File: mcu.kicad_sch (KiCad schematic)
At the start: 15 parts, among them J3 PinHeader_2x05, U4 ISP1807-LR-RS, U5 D3V3XA4B10LP

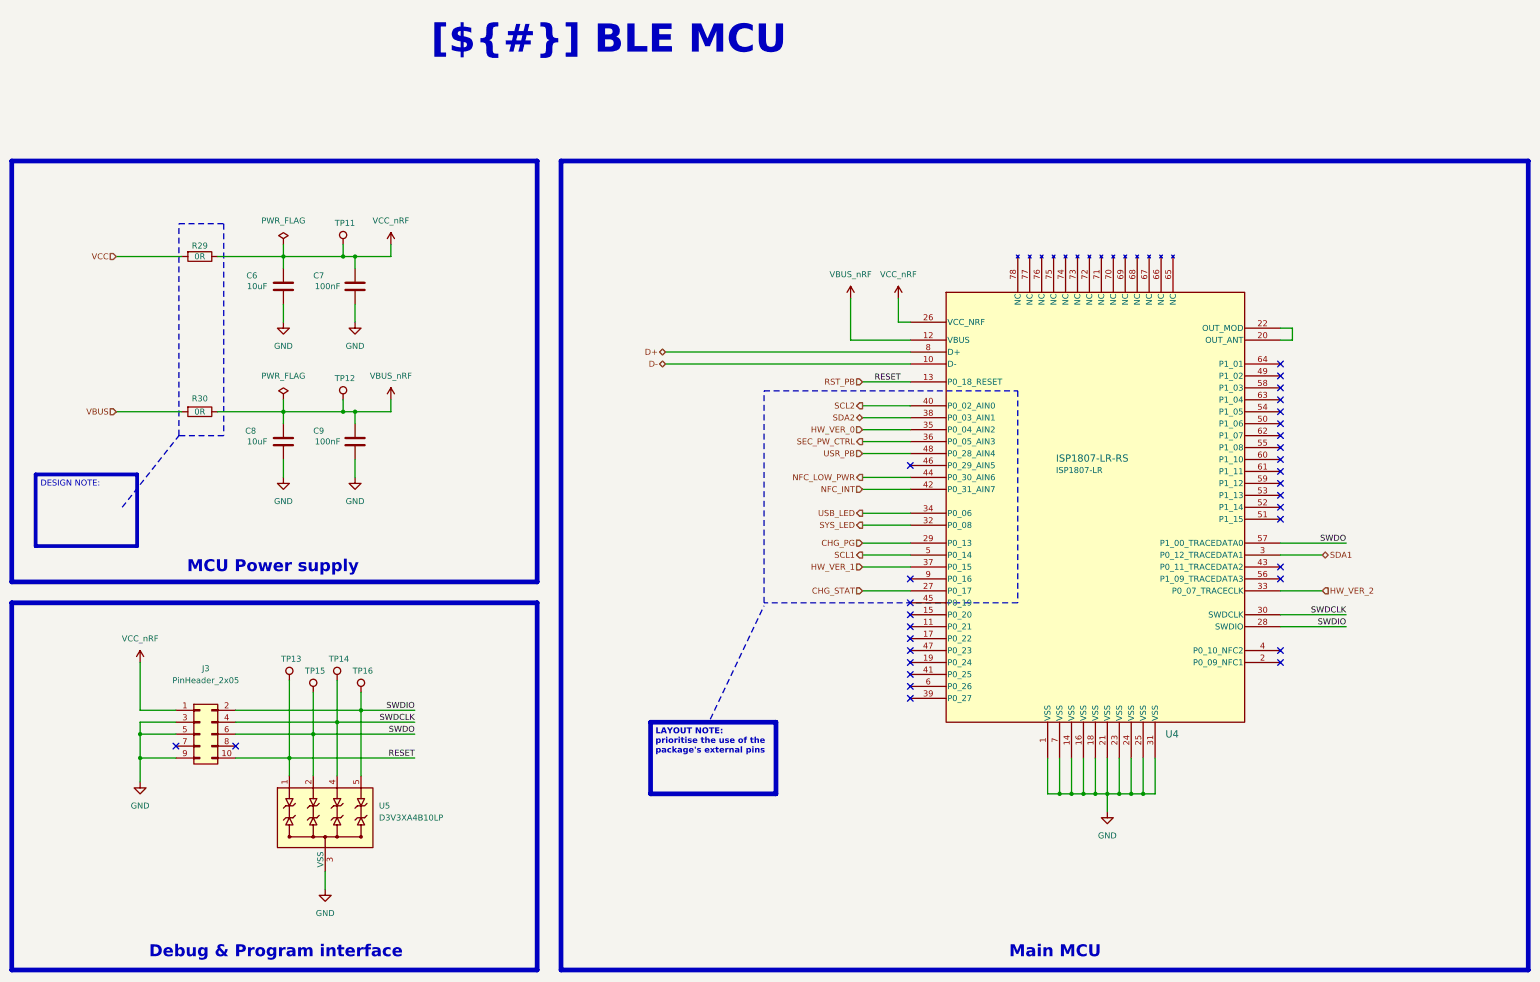
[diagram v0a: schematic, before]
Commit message: fix(hardware): replace jumper/passive footprints with 0402 and refine schematics
- Replace 0-ohm jumper resistors with 0402 package equivalents
- Reduce package size on several capacitors
- Correct and simplify several schematic symbols (replaced with
  simplified equivalents where the original was overcomplicated)
- Bump lib submodule to the updated component library (renamed
  switch footprints, new Conn_01x02_MountingPin symbol, pad/pin
  numbering fixes, approved IPN assignments, Workart artwork library)
- Register Workart.pretty in fp-lib-table
- Mark J3 as DNP in mcu.kicad_sch
- Continue schematic wiring/placement (Leds.kicad_sch, tessera.kicad_sch)
  and PCB routing/placement (tessera.kicad_pcb)
- Add board outline source (Images/pcb_size.dxf, pcb_shape.FCStd) and
  silkscreen artwork sources (Logos/) for the Workart footprints
- Complete preliminary version of PCB
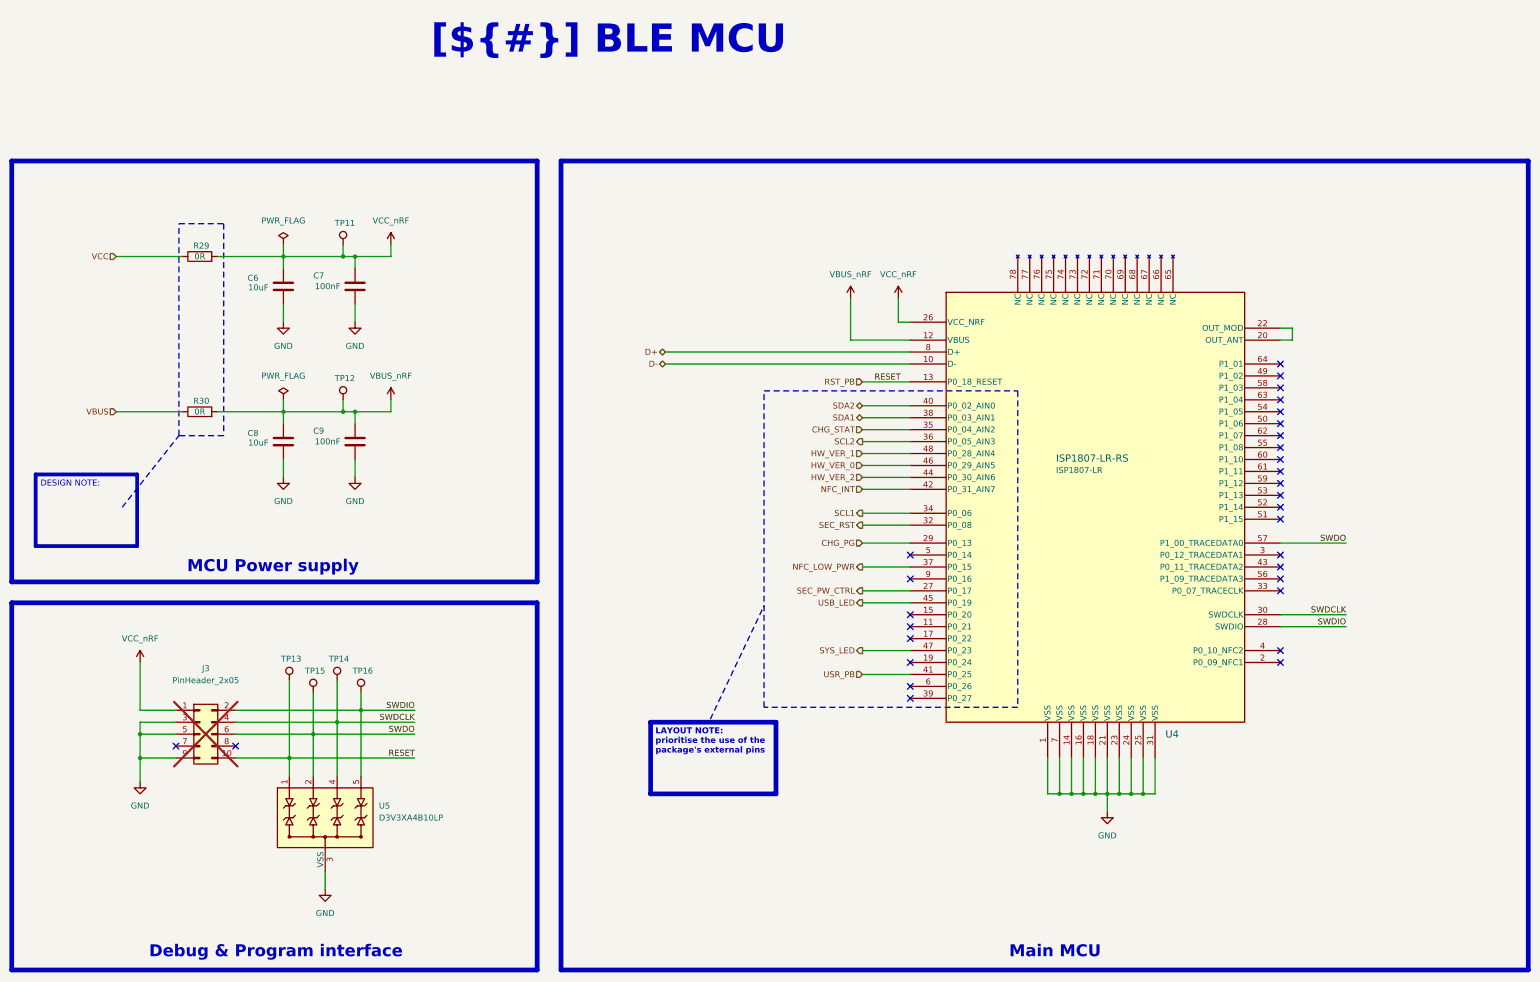
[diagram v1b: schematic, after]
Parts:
- removed C6, C8: 10uF 50V (X7R), Capacitor_SMD:C_1210_3225Metric, symbol catalog:Capacitors/C1210_10uF_50V_±10%_X7R
- removed R29, R30: 0R ±5% 1/10W, Resistor_SMD:R_0603_1608Metric, symbol catalog:Resistors/R0603_0R_0.1W_±5%
- added C6, C8: 10uF 10V (X7R), Capacitor_SMD:C_0805_2012Metric, symbol catalog:Capacitors/C0805_10uF_10V_±10%_X7R
- added R29, R30: 0R ±5% 1/16W, Resistor_SMD:R_0402_1005Metric, symbol catalog:Resistors/R0402_0R_0.1W_±5%
- J3: now not fitted
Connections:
- net CHG_STAT: now also U4.35 (P0_04_AIN2); no longer U4.27 (P0_17)
- net GND: now also C6.2, C8.2
- net HW_VER_0: now also U4.46 (P0_29_AIN5); no longer U4.35 (P0_04_AIN2)
- net HW_VER_1: now also U4.48 (P0_28_AIN4); no longer U4.37 (P0_15)
- net HW_VER_2: now also U4.44 (P0_30_AIN6); no longer U4.33 (P0_07_TRACECLK)
- net NFC_LOW_PWR: now also U4.37 (P0_15); no longer U4.44 (P0_30_AIN6)
- net SCL1: now also U4.34 (P0_06); no longer U4.5 (P0_14)
- net SCL2: now also U4.36 (P0_05_AIN3); no longer U4.40 (P0_02_AIN0)
- net SDA1: now also U4.38 (P0_03_AIN1); no longer U4.3 (P0_12_TRACEDATA1)
- net SDA2: now also U4.40 (P0_02_AIN0); no longer U4.38 (P0_03_AIN1)
- net SEC_PW_CTRL: now also U4.27 (P0_17); no longer U4.36 (P0_05_AIN3)
- net SWDIO: now also U5.6; no longer U5.10
- net SYS_LED: now also U4.47 (P0_23); no longer U4.32 (P0_08)
- net USB_LED: now also U4.45 (P0_19); no longer U4.34 (P0_06)
- net USR_PB: now also U4.41 (P0_25); no longer U4.48 (P0_28_AIN4)
- net VBUS: now also R30.1
- net VBUS_nRF: now also C8.1, R30.2
- net VCC: now also R29.1
- net VCC_nRF: now also C6.1, R29.2
- new net SEC_RST: U4.32 (P0_08)
- no-connect marks 31 -> 30

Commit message: feat(hardware): route debug UART to J3 and add charger status pull-ups
Exposes a spare UART on the SWD header for firmware logging and adds
external pull-ups to the BQ25170 open-drain status outputs.

- Route P0.22 (UART_TX) to J3 pin 7 and P0.20 (UART_RX) to J3 pin 8.
- Add R44/R45 100k pull-ups to VCC on CHG_STAT and CHG_PG.
- Update PCB placement and routing for the new nets.
- Bump lib submodule (new THT test point footprint).
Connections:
- net UART_RX: now reaches U4.15 (P0_20)
- net UART_RX: now also J3.8 (Pin_8)
- net UART_TX: now reaches U4.17 (P0_22)
- net UART_TX: now also J3.7 (Pin_7)
- no-connect marks 30 -> 26
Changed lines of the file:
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@@
 	(title_block
 		(title "BLE MCU")
-		(date "2026-10-03")
+		(date "2026-10-11")
 	)
 	(junction
@@
 	)
 	(no_connect
-		(at 245.11 158.75)
-	)
-	(no_connect
 		(at 323.85 143.51)
 	)
@@
 	)
 	(no_connect
-		(at 88.9 181.61)
-	)
-	(no_connect
 		(at 323.85 107.95)
 	)
@@
 	)
 	(no_connect
-		(at 101.6 181.61)
-	)
-	(no_connect
 		(at 245.11 163.83)
 	)
 	(no_connect
-		(at 245.11 153.67)
-	)
-	(no_connect
 		(at 323.85 102.87)
 	)
@@
 	(wire
 		(pts
-			(xy 234.95 134.62) (xy 245.11 134.62)
-		)
-		(stroke
-			(width 0)
-			(type default)
-		)
-	)
-	(wire
-		(pts
-			(xy 234.95 143.51) (xy 245.11 143.51)
+			(xy 232.41 134.62) (xy 245.11 134.62)
+		)
+		(stroke
+			(width 0)
+			(type default)
+		)
+	)
+	(wire
+		(pts
+			(xy 232.41 143.51) (xy 245.11 143.51)
 		)
 		(stroke
@@
 	(wire
 		(pts
-			(xy 234.95 151.13) (xy 245.11 151.13)
+			(xy 232.41 151.13) (xy 245.11 151.13)
+		)
+		(stroke
+			(width 0)
+			(type default)
+		)
+	)
+	(wire
+		(pts
+			(xy 69.85 181.61) (xy 88.9 181.61)
 		)
 		(stroke
@@
 	(wire
 		(pts
-			(xy 245.11 124.46) (xy 234.95 124.46)
+			(xy 245.11 124.46) (xy 232.41 124.46)
 		)
 		(stroke
@@
 	(wire
 		(pts
-			(xy 234.95 116.84) (xy 245.11 116.84)
-		)
-		(stroke
-			(width 0)
-			(type default)
-		)
-	)
-	(wire
-		(pts
-			(xy 234.95 119.38) (xy 245.11 119.38)
+			(xy 232.41 116.84) (xy 245.11 116.84)
+		)
+		(stroke
+			(width 0)
+			(type default)
+		)
+	)
+	(wire
+		(pts
+			(xy 232.41 119.38) (xy 245.11 119.38)
 		)
 		(stroke
@@
 	(wire
 		(pts
-			(xy 234.95 161.29) (xy 245.11 161.29)
+			(xy 232.41 161.29) (xy 245.11 161.29)
 		)
 		(stroke
@@
 	(wire
 		(pts
-			(xy 234.95 132.08) (xy 245.11 132.08)
+			(xy 232.41 132.08) (xy 245.11 132.08)
 		)
 		(stroke
@@
 	(wire
 		(pts
-			(xy 234.95 111.76) (xy 245.11 111.76)
+			(xy 232.41 111.76) (xy 245.11 111.76)
 		)
 		(stroke
@@
 	(wire
 		(pts
-			(xy 234.95 138.43) (xy 245.11 138.43)
+			(xy 232.41 138.43) (xy 245.11 138.43)
 		)
 		(stroke
@@
 	(wire
 		(pts
-			(xy 234.95 114.3) (xy 245.11 114.3)
+			(xy 232.41 114.3) (xy 245.11 114.3)
 		)
 		(stroke
@@
 	(wire
 		(pts
+			(xy 234.95 153.67) (xy 245.11 153.67)
+		)
+		(stroke
+			(width 0)
+			(type default)
+		)
+	)
+	(wire
+		(pts
 			(xy 111.76 77.47) (xy 111.76 80.01)
 		)
@@
 	(wire
 		(pts
-			(xy 234.95 166.37) (xy 245.11 166.37)
+			(xy 232.41 166.37) (xy 245.11 166.37)
 		)
 		(stroke
@@
 	(wire
 		(pts
-			(xy 234.95 127) (xy 245.11 127)
+			(xy 232.41 127) (xy 245.11 127)
+		)
+		(stroke
+			(width 0)
+			(type default)
+		)
+	)
+	(wire
+		(pts
+			(xy 234.95 158.75) (xy 245.11 158.75)
 		)
 		(stroke
@@
 	(wire
 		(pts
-			(xy 234.95 148.59) (xy 245.11 148.59)
+			(xy 232.41 148.59) (xy 245.11 148.59)
 		)
 		(stroke
@@
 	(wire
 		(pts
+			(xy 101.6 181.61) (xy 139.7 181.61)
+		)
+		(stroke
+			(width 0)
+			(type default)
+		)
+	)
+	(wire
+		(pts
 			(xy 274.32 191.77) (xy 276.86 191.77)
 		)
@@
 	(wire
 		(pts
-			(xy 234.95 109.22) (xy 245.11 109.22)
+			(xy 232.41 109.22) (xy 245.11 109.22)
 		)
 		(stroke
@@
 	(wire
 		(pts
-			(xy 234.95 121.92) (xy 245.11 121.92)
+			(xy 232.41 121.92) (xy 245.11 121.92)
 		)
 		(stroke
@@
 		)
 	)
+	(label "UART_RX"
+		(at 234.95 153.67 0)
+		(fields_autoplaced yes)
+		(effects
+			(font
+				(size 1.27 1.27)
+			)
+			(justify left bottom)
+		)
+	)
 	(label "SWDCLK"
 		(at 337.82 153.67 180)
@@
 		)
 	)
+	(label "UART_RX"
+		(at 139.7 181.61 180)
+		(fields_autoplaced yes)
+		(effects
+			(font
+				(size 1.27 1.27)
+			)
+			(justify right bottom)
+		)
+	)
 	(label "RESET"
 		(at 237.49 104.14 0)
@@
 		)
 	)
+	(label "UART_TX"
+		(at 234.95 158.75 0)
+		(fields_autoplaced yes)
+		(effects
+			(font
+				(size 1.27 1.27)
+			)
+			(justify left bottom)
+		)
+	)
 	(label "SWDCLK"
 		(at 139.7 176.53 180)
@@
 		)
 	)
+	(label "UART_TX"
+		(at 69.85 181.61 0)
+		(fields_autoplaced yes)
+		(effects
+			(font
+				(size 1.27 1.27)
+			)
+			(justify left bottom)
+		)
+	)
 	(label "SWDO"
 		(at 337.82 138.43 180)
@@
 	(hierarchical_label "SYS_LED"
 		(shape output)
-		(at 234.95 161.29 180)
+		(at 232.41 161.29 180)
 		(fields_autoplaced yes)
 		(effects
@@
 	(hierarchical_label "SCL2"
 		(shape output)
-		(at 234.95 116.84 180)
+		(at 232.41 116.84 180)
 		(fields_autoplaced yes)
 		(effects
@@
 	(hierarchical_label "CHG_PG"
 		(shape input)
-		(at 234.95 138.43 180)
+		(at 232.41 138.43 180)
 		(fields_autoplaced yes)
 		(effects
@@
 	(hierarchical_label "SEC_RST"
 		(shape output)
-		(at 234.95 134.62 180)
+		(at 232.41 134.62 180)
 		(fields_autoplaced yes)
 		(effects
@@
 	(hierarchical_label "NFC_INT"
 		(shape input)
-		(at 234.95 127 180)
+		(at 232.41 127 180)
 		(fields_autoplaced yes)
 		(effects
@@
 	(hierarchical_label "SDA2"
 		(shape bidirectional)
-		(at 234.95 109.22 180)
+		(at 232.41 109.22 180)
 		(fields_autoplaced yes)
 		(effects
@@
 	(hierarchical_label "USB_LED"
 		(shape output)
-		(at 234.95 151.13 180)
+		(at 232.41 151.13 180)
 		(fields_autoplaced yes)
 		(effects
@@
 	(hierarchical_label "SEC_PW_CTRL"
 		(shape output)
-		(at 234.95 148.59 180)
+		(at 232.41 148.59 180)
 		(fields_autoplaced yes)
 		(effects
@@
 	(hierarchical_label "USR_PB"
 		(shape input)
-		(at 234.95 166.37 180)
+		(at 232.41 166.37 180)
 		(fields_autoplaced yes)
 		(effects
@@
 	(hierarchical_label "NFC_LOW_PWR"
 		(shape output)
-		(at 234.95 143.51 180)
+		(at 232.41 143.51 180)
 		(fields_autoplaced yes)
 		(effects
@@
 	(hierarchical_label "HW_VER_0"
 		(shape input)
-		(at 234.95 121.92 180)
+		(at 232.41 121.92 180)
 		(fields_autoplaced yes)
 		(effects
@@
 	(hierarchical_label "CHG_STAT"
 		(shape input)
-		(at 234.95 114.3 180)
+		(at 232.41 114.3 180)
 		(fields_autoplaced yes)
 		(effects
@@
 	(hierarchical_label "SDA1"
 		(shape bidirectional)
-		(at 234.95 111.76 180)
+		(at 232.41 111.76 180)
 		(fields_autoplaced yes)
 		(effects
@@
 	(hierarchical_label "HW_VER_2"
 		(shape input)
-		(at 234.95 124.46 180)
+		(at 232.41 124.46 180)
 		(fields_autoplaced yes)
 		(effects
@@
 	(hierarchical_label "HW_VER_1"
 		(shape input)
-		(at 234.95 119.38 180)
+		(at 232.41 119.38 180)
 		(fields_autoplaced yes)
 		(effects
@@
 	(hierarchical_label "SCL1"
 		(shape output)
-		(at 234.95 132.08 180)
-		(fields_autoplaced yes)
-		(effects
+		(at 232.41 132.08 180)
+		(fields_autoplaced yes)
+		(effects
